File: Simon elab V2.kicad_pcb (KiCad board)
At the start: 2 copper layers, 23 parts, among them SW1 SW_SPST, SW2 SW_Push, SW3 SW_Push, SW4 SW_Push, SW5 SW_Push, U1 ATtiny13A-P

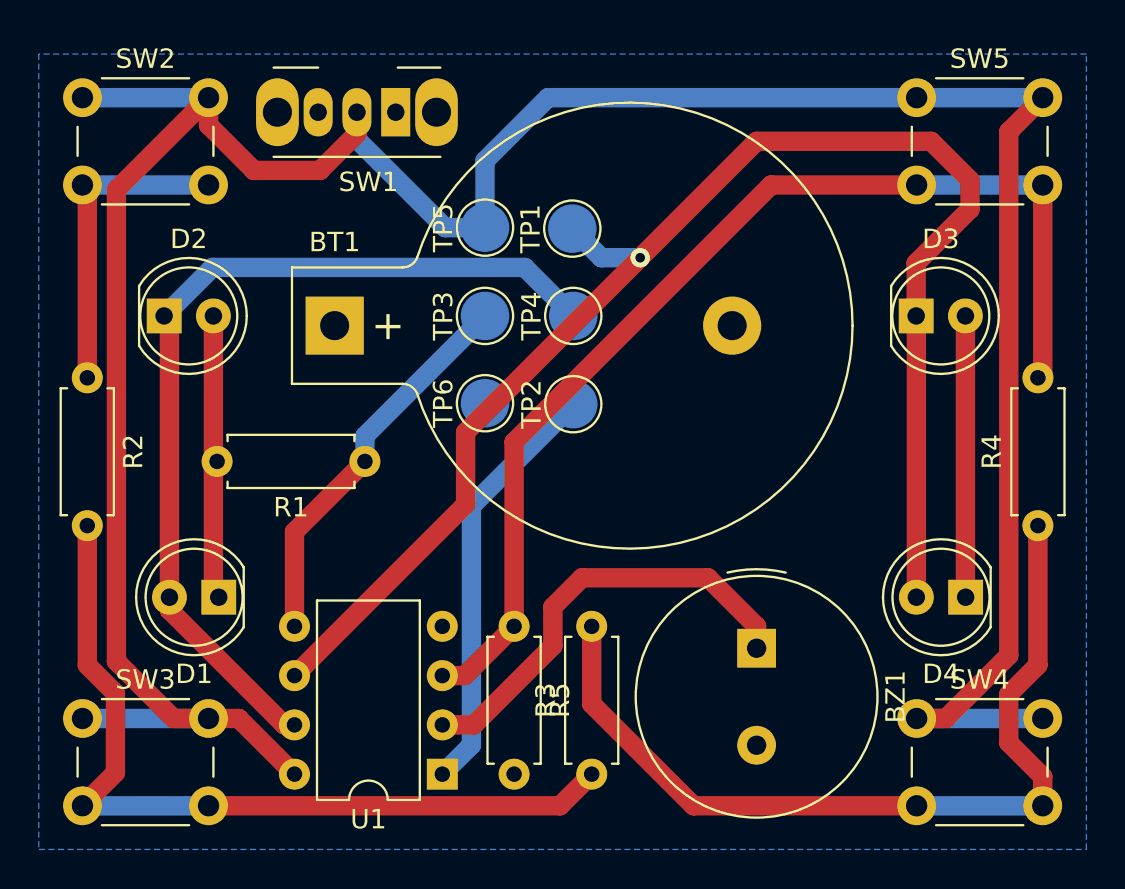
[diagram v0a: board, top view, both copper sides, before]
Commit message: Silk screen and edge cuts edit
Silk screen
Edge cuts
Adding DNG filled zone F.Cu
Correcting TP at bottom layer
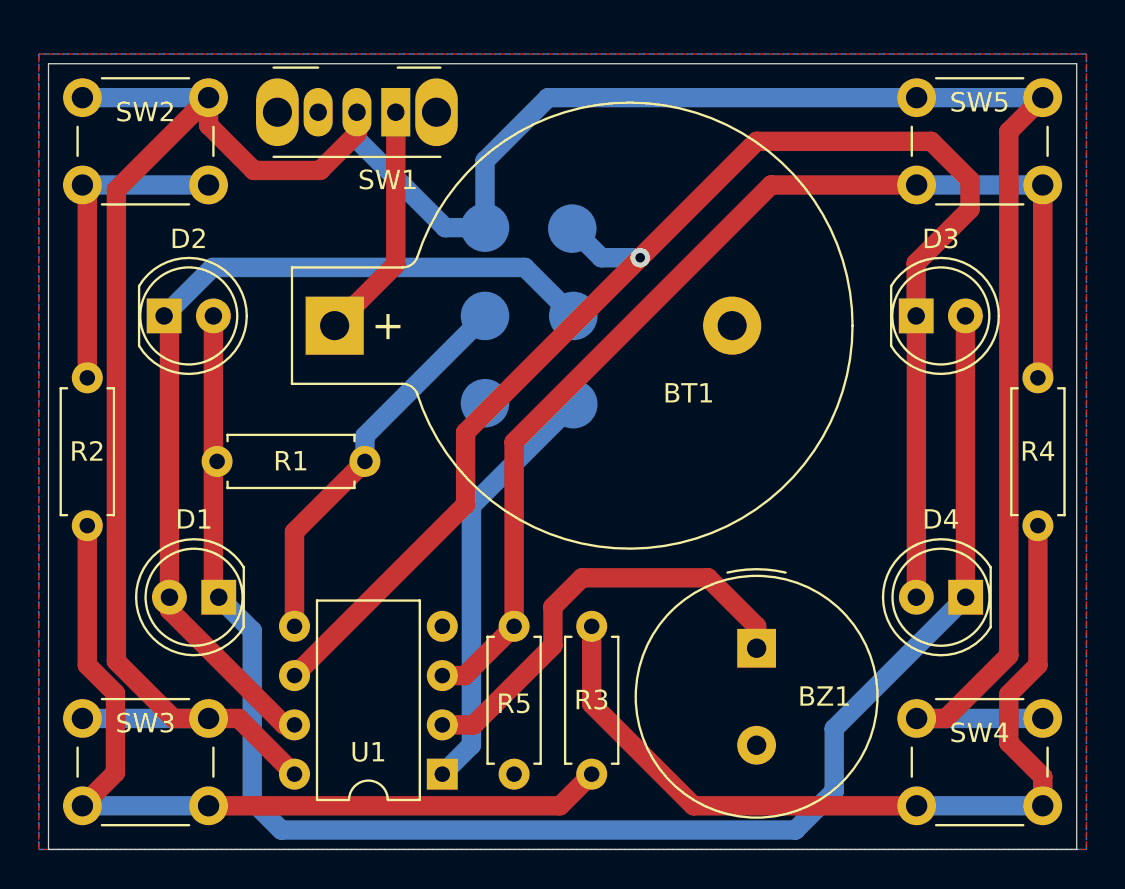
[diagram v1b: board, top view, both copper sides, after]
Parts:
- TP1, TP2, TP3, TP4, TP5, TP6: moved to B.Cu
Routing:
- net Net-(D1-K): track 29.1 -> 84.6 mm
- net Net-(BT1-+): track 0.00 -> 12.3 mm
- added copper zone on F.Cu, net GND
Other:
- board outline added: 53 x 40.5 mm
- board text added: "Simon electroLAB - UMONS Yann Jacquet 2024_05_03"

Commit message: V1.0 Gerber creation
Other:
- board text added: "Simon V1.0 electroLAB - UMONS Yann Jacquet 2024_05_03"
- board text removed: "Simon electroLAB - UMONS Yann Jacquet 2024_05_03"
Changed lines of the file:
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@@
 			(plot_on_all_layers_selection 0x0000000_00000000)
 			(disableapertmacros no)
-			(usegerberextensions no)
-			(usegerberattributes yes)
-			(usegerberadvancedattributes yes)
-			(creategerberjobfile yes)
+			(usegerberextensions yes)
+			(usegerberattributes no)
+			(usegerberadvancedattributes no)
+			(creategerberjobfile no)
 			(dashed_line_dash_ratio 12.000000)
 			(dashed_line_gap_ratio 3.000000)
@@
 			(psa4output no)
 			(plotreference yes)
-			(plotvalue yes)
+			(plotvalue no)
 			(plotfptext yes)
 			(plotinvisibletext no)
 			(sketchpadsonfab no)
-			(subtractmaskfromsilk no)
+			(subtractmaskfromsilk yes)
 			(outputformat 1)
 			(mirror no)
-			(drillshape 1)
+			(drillshape 0)
 			(scaleselection 1)
-			(outputdirectory "")
+			(outputdirectory "Gerber V1.0/")
 		)
 	)
@@
 		(fp_arc
 			(start 3.5 3.25)
-			(mid 3.80926 3.345922)
+			(mid 3.809266 3.345926)
 			(end 4.01 3.6)
 			(stroke
@@
 		)
 		(property "Value" "TP_VCC"
-			(at 0 -2.25 270)
+			(at 0 -2.25 -90)
 			(layer "B.Fab")
 			(effects
@@
 		)
 		(fp_text user "${REFERENCE}"
-			(at 0 2.15 270)
+			(at 0 2.15 -90)
 			(layer "B.Fab")
 			(effects
@@
 		)
 		(property "Value" "TP_MISO"
-			(at 0 -2.25 270)
+			(at 0 -2.25 -90)
 			(layer "B.Fab")
 			(effects
@@
 		)
 		(fp_text user "${REFERENCE}"
-			(at 0 2.15 270)
+			(at 0 2.15 -90)
 			(layer "B.Fab")
 			(effects
@@
 		)
 		(property "Value" "TP_GND"
-			(at 0 -2.25 270)
+			(at 0 -2.25 -90)
 			(layer "B.Fab")
 			(effects
@@
 		)
 		(fp_text user "${REFERENCE}"
-			(at 0 2.15 270)
+			(at 0 2.15 -90)
 			(layer "B.Fab")
 			(effects
@@
 		)
 		(property "Value" "TP_MOSI"
-			(at 0 -2.25 270)
+			(at 0 -2.25 -90)
 			(layer "B.Fab")
 			(effects
@@
 		)
 		(fp_text user "${REFERENCE}"
-			(at 0 2.15 270)
+			(at 0 2.15 -90)
 			(layer "B.Fab")
 			(effects
@@
 		)
 		(property "Value" "TP_CLOCK"
-			(at 0 -2.25 270)
+			(at 0 -2.25 -90)
 			(layer "B.Fab")
 			(effects
@@
 		)
 		(fp_text user "${REFERENCE}"
-			(at 0 2.15 270)
+			(at 0 2.15 -90)
 			(layer "B.Fab")
 			(effects
@@
 		)
 		(property "Value" "TP_RST"
-			(at 0 -2.25 270)
+			(at 0 -2.25 -90)
 			(layer "B.Fab")
 			(effects
@@
 		)
 		(fp_text user "${REFERENCE}"
-			(at 0 2.15 270)
+			(at 0 2.15 -90)
 			(layer "B.Fab")
 			(effects
@@
 		(layer "Edge.Cuts")
 	)
-	(gr_text "Simon\nelectroLAB - UMONS\nYann Jacquet 2024_05_03"
+	(gr_text "Simon V1.0\nelectroLAB - UMONS\nYann Jacquet 2024_05_03"
 		(at 134 124.5 0)
 		(layer "B.SilkS")
